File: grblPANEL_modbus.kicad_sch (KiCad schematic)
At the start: 16 parts, among them J401 Conn_01x02, U401 THVD1406

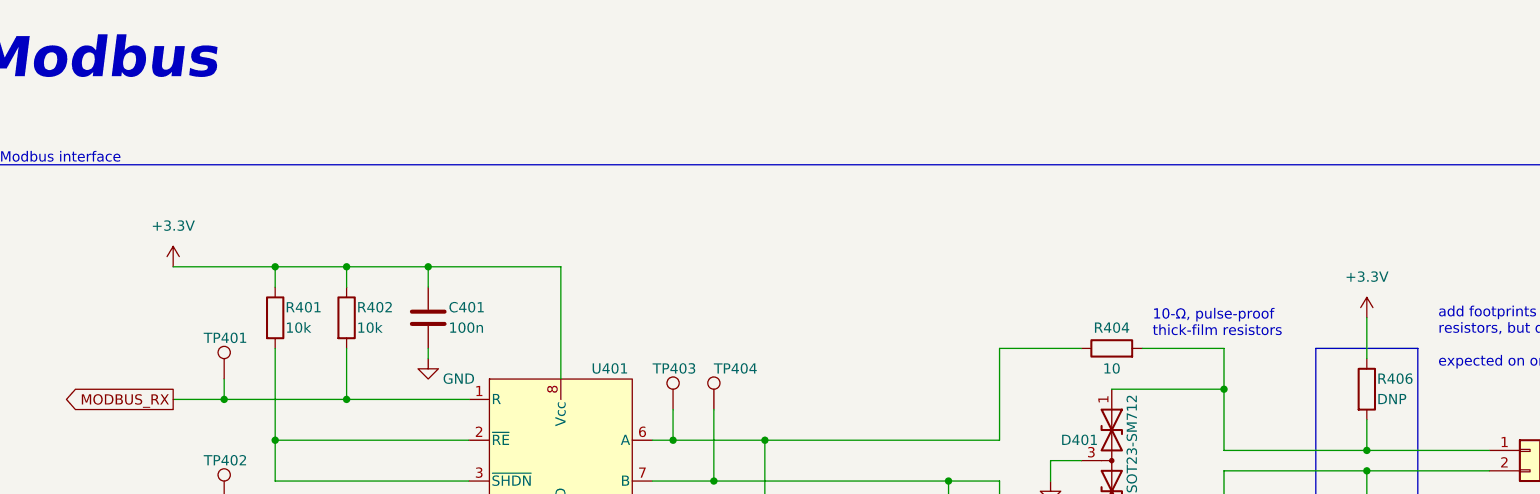
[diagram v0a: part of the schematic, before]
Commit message: ERC fixes
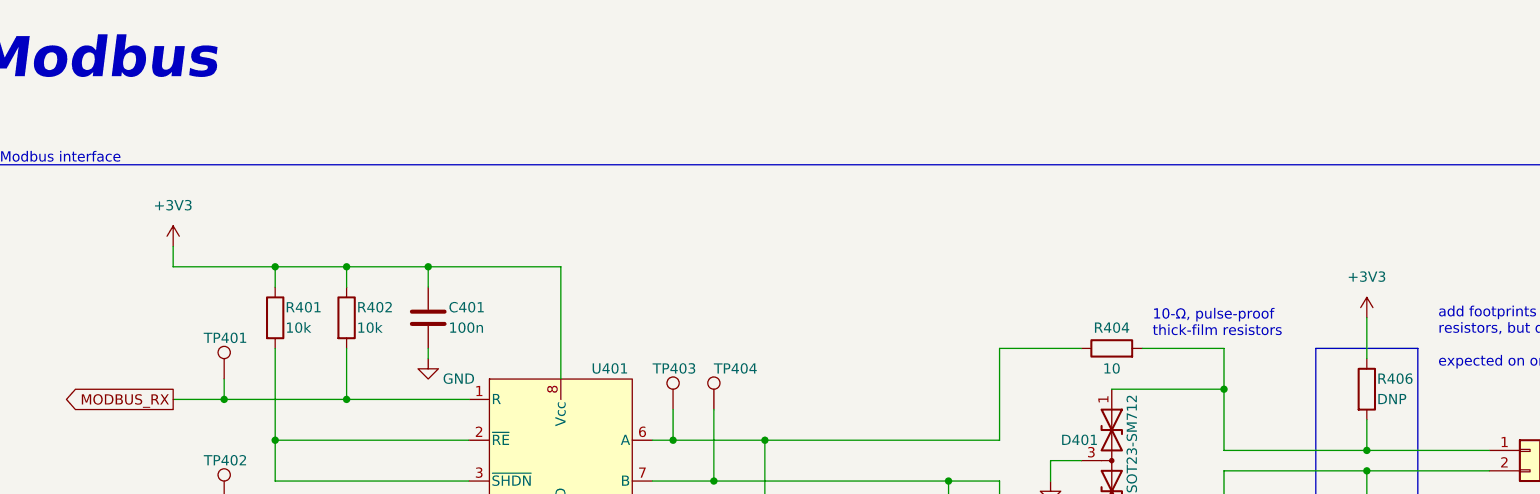
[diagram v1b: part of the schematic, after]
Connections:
- net +3.3V renamed +3V3
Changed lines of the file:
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@@
+    (stroke (width 0) (type default) (color 0 0 0 0))
+  )
+  (wire (pts (xy 62.23 49.53) (xy 62.23 52.07))
     (stroke (width 0) (type default) (color 0 0 0 0))
   )
@@
     (pin "1")
     (pin "2")
-  )
-  (symbol (lib_id "power:+3.3V") (at 210.82 58.42 0) (unit 1)
-    (in_bom yes) (on_board yes) (fields_autoplaced)
-    (property "Reference" "#PWR0405" (id 0) (at 210.82 62.23 0)
-      (effects (font (size 1.27 1.27)) hide)
-    )
-    (property "Value" "+3.3V" (id 1) (at 210.82 53.34 0))
-    (property "Footprint" "" (id 2) (at 210.82 58.42 0)
-      (effects (font (size 1.27 1.27)) hide)
-    )
-    (property "Datasheet" "" (id 3) (at 210.82 58.42 0)
-      (effects (font (size 1.27 1.27)) hide)
-    )
-    (pin "1")
   )
   (symbol (lib_id "Connector_Generic:Conn_01x02") (at 231.14 74.93 0) (unit 1)
@@
     (pin "1")
   )
+  (symbol (lib_id "power:+3V3") (at 62.23 49.53 0) (unit 1)
+    (in_bom yes) (on_board yes) (fields_autoplaced)
+    (property "Reference" "#PWR0108" (id 0) (at 62.23 53.34 0)
+      (effects (font (size 1.27 1.27)) hide)
+    )
+    (property "Value" "+3V3" (id 1) (at 62.23 44.45 0))
+    (property "Footprint" "" (id 2) (at 62.23 49.53 0)
+      (effects (font (size 1.27 1.27)) hide)
+    )
+    (property "Datasheet" "" (id 3) (at 62.23 49.53 0)
+      (effects (font (size 1.27 1.27)) hide)
+    )
+    (pin "1")
+  )
   (symbol (lib_id "Device:R") (at 179.07 62.23 90) (unit 1)
     (in_bom yes) (on_board yes)
@@
     (pin "3")
   )
-  (symbol (lib_id "power:+3.3V") (at 62.23 52.07 0) (unit 1)
-    (in_bom yes) (on_board yes) (fields_autoplaced)
-    (property "Reference" "#PWR0401" (id 0) (at 62.23 55.88 0)
-      (effects (font (size 1.27 1.27)) hide)
-    )
-    (property "Value" "+3.3V" (id 1) (at 62.23 46.99 0))
-    (property "Footprint" "" (id 2) (at 62.23 52.07 0)
-      (effects (font (size 1.27 1.27)) hide)
-    )
-    (property "Datasheet" "" (id 3) (at 62.23 52.07 0)
-      (effects (font (size 1.27 1.27)) hide)
-    )
-    (pin "1")
-  )
   (symbol (lib_id "Connector:TestPoint") (at 124.46 69.85 0) (unit 1)
     (in_bom yes) (on_board yes)
@@
     (pin "2")
   )
+  (symbol (lib_id "power:+3V3") (at 210.82 58.42 0) (unit 1)
+    (in_bom yes) (on_board yes) (fields_autoplaced)
+    (property "Reference" "#PWR0109" (id 0) (at 210.82 62.23 0)
+      (effects (font (size 1.27 1.27)) hide)
+    )
+    (property "Value" "+3V3" (id 1) (at 210.82 53.34 0))
+    (property "Footprint" "" (id 2) (at 210.82 58.42 0)
+      (effects (font (size 1.27 1.27)) hide)
+    )
+    (property "Datasheet" "" (id 3) (at 210.82 58.42 0)
+      (effects (font (size 1.27 1.27)) hide)
+    )
+    (pin "1")
+  )
   (symbol (lib_id "power:GND") (at 171.45 78.74 0) (unit 1)

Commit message: Refresh
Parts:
- C401: footprint (none) -> Capacitor_SMD:C_0603_1608Metric
- D401: footprint (none) -> Package_TO_SOT_SMD:SOT-23
- J401: footprint (none) -> TerminalBlock_4Ucon:TerminalBlock_4Ucon_1x02_P3.50mm_Horizontal
- JP401, TP401, TP402, TP403, TP404: footprint (none) -> Connector_Pin:Pin_D1.0mm_L10.0mm
- R401, R402, R403, R406, R407: footprint (none) -> Resistor_SMD:R_0603_1608Metric
- R404, R405: footprint (none) -> Resistor_SMD:R_1206_3216Metric
- U401: footprint (none) -> Package_SO:SOIC-8_3.9x4.9mm_P1.27mm
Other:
- note added: "1/2 watt termination resistor"
- note added: "Add footprints for 570 ohm bias resistors, but do not populate. Should be present on only one modbus node (usually master)."
- note added: "SM712 TVS - Vrwm -7v, +12v - Vbr -7.5v, +13.3v - Vc -10v, +19v (@ 1A) THVD106 - Max bus voltage +/- 12v - Peak bus voltage +/- 16v - ESD rated +/- 16kv"
- note added: "THVD1406 - 3.3v, auto switching (and mostly out of stock..) Enable auto-direction mode by tying SHDN and RE pins together to logic high"
- note added: "THVD1406 - 3.3v, auto switching, mostly out of stock.."
- note removed: "Enable auto-direction mode by tying SHDN and RE pins together to logic high"
- note removed: "THVD1406 - 3.3v, auto switching, mostly out of stock.. todo: take a closer look at the circuitry of existing AliExpress adapter"
- note removed: "add footprints for 570 ohm bias resistors, but do not populate. expected on only single (master) node"
- moved on the sheet: D401, J401, R404, R405, R406, R407

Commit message: PCB layout - WIP
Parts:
- J401: footprint TerminalBlock_4Ucon:TerminalBlock_4Ucon_1x02_P3.50mm_Horizontal -> TerminalBlock_Phoenix:TerminalBlock_Phoenix_PT-1,5-2-3.5-H_1x02_P3.50mm_Horizontal
- JP401: footprint Connector_Pin:Pin_D1.0mm_L10.0mm -> Connector_PinHeader_2.54mm:PinHeader_1x02_P2.54mm_Vertical
- TP401, TP402, TP403, TP404: footprint Connector_Pin:Pin_D1.0mm_L10.0mm -> TestPoint:TestPoint_THTPad_D2.0mm_Drill1.0mm
- renumbered R406 to R404, R407 to R405, R404 to R406, R405 to R407
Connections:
- net CONN_RS485_A: now reaches D401.1 (A1), J401.1 (Pin_1), R406.2
- net CONN_RS485_A: no longer R404.2
- net CONN_RS485_B: now reaches D401.2 (A2), J401.2 (Pin_2), R407.2
- net CONN_RS485_B: no longer R405.1
- net RS485_B: now reaches JP401.2 (B), R407.1, TP404.1, U401.7 (B)
- net RS485_B: now also R405.1
- net RS485_MODE_SELECT: now reaches R401.2, U401.2 (~{RE}), U401.3 (~{SHDN})
- net RS485_A: now reaches R403.1, R406.1, TP403.1, U401.6 (A)
- net RS485_A: now also R404.2
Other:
- moved on the sheet: D401, J401, R404, R405, R406, R407

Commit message: modbus cleanup
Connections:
- net CONN_RS485_A: now also D401.2 (A2); no longer D401.1 (A1)
- net CONN_RS485_B: now also D401.1 (A1); no longer D401.2 (A2)
- net RS485_A: now also JP401.1 (A); no longer R403.1
- net RS485_B: now also R403.2; no longer JP401.2 (B)
- new net: JP401.2 (B), R403.1
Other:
- moved on the sheet: JP401, R403
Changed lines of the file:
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@@
     (stroke (width 0) (type default) (color 0 0 0 0))
   )
-  (wire (pts (xy 144.78 85.09) (xy 147.32 85.09))
+  (wire (pts (xy 147.32 85.09) (xy 149.86 85.09))
     (stroke (width 0) (type default) (color 0 0 0 0))
   )
@@
     (pin "8")
   )
-  (symbol (lib_id "Device:R") (at 140.97 85.09 90) (unit 1)
-    (in_bom yes) (on_board yes)
-    (property "Reference" "R403" (id 0) (at 140.97 82.55 90))
-    (property "Value" "120" (id 1) (at 140.97 87.63 90))
-    (property "Footprint" "Resistor_SMD:R_0603_1608Metric" (id 2) (at 140.97 86.868 90)
-      (effects (font (size 1.27 1.27)) hide)
-    )
-    (property "Datasheet" "~" (id 3) (at 140.97 85.09 0)
+  (symbol (lib_id "Device:R") (at 153.67 85.09 90) (unit 1)
+    (in_bom yes) (on_board yes)
+    (property "Reference" "R403" (id 0) (at 153.67 82.55 90))
+    (property "Value" "120" (id 1) (at 153.67 87.63 90))
+    (property "Footprint" "Resistor_SMD:R_0603_1608Metric" (id 2) (at 153.67 86.868 90)
+      (effects (font (size 1.27 1.27)) hide)
+    )
+    (property "Datasheet" "~" (id 3) (at 153.67 85.09 0)
       (effects (font (size 1.27 1.27)) hide)
     )
@@
     (pin "1")
   )
-  (symbol (lib_id "Device:D_TVS_Dual_AAC") (at 208.28 76.2 270) (unit 1)
-    (in_bom yes) (on_board yes)
-    (property "Reference" "D401" (id 0) (at 201.93 73.66 90)
-      (effects (font (size 1.27 1.27)) (justify left))
-    )
-    (property "Value" "CDSOT23-SM712" (id 1) (at 210.82 67.945 0)
-      (effects (font (size 1.27 1.27)) (justify left))
-    )
-    (property "Footprint" "Package_TO_SOT_SMD:SOT-23" (id 2) (at 208.28 72.39 0)
-      (effects (font (size 1.27 1.27)) hide)
-    )
-    (property "Datasheet" "~" (id 3) (at 208.28 72.39 0)
+  (symbol (lib_id "Device:D_TVS_Dual_AAC") (at 208.28 76.2 270) (mirror x) (unit 1)
+    (in_bom yes) (on_board yes)
+    (property "Reference" "D401" (id 0) (at 201.93 78.74 90)
+      (effects (font (size 1.27 1.27)) (justify left))
+    )
+    (property "Value" "CDSOT23-SM712" (id 1) (at 210.82 84.455 0)
+      (effects (font (size 1.27 1.27)) (justify left))
+    )
+    (property "Footprint" "Package_TO_SOT_SMD:SOT-23" (id 2) (at 208.28 80.01 0)
+      (effects (font (size 1.27 1.27)) hide)
+    )
+    (property "Datasheet" "~" (id 3) (at 208.28 80.01 0)
       (effects (font (size 1.27 1.27)) hide)
     )
@@
     (pin "2")
   )
-  (symbol (lib_id "Jumper:Jumper_2_Bridged") (at 152.4 85.09 0) (unit 1)
-    (in_bom yes) (on_board yes)
-    (property "Reference" "JP401" (id 0) (at 152.4 82.55 0))
-    (property "Value" "Jumper_2_Bridged" (id 1) (at 156.21 87.63 0)
-      (effects (font (size 1.27 1.27)) hide)
-    )
-    (property "Footprint" "Connector_PinHeader_2.54mm:PinHeader_1x02_P2.54mm_Vertical" (id 2) (at 152.4 85.09 0)
-      (effects (font (size 1.27 1.27)) hide)
-    )
-    (property "Datasheet" "~" (id 3) (at 152.4 85.09 0)
-      (effects (font (size 1.27 1.27)) hide)
-    )
+  (symbol (lib_id "Jumper:Jumper_2_Bridged") (at 142.24 85.09 0) (unit 1)
+    (in_bom yes) (on_board yes)
+    (property "Reference" "JP401" (id 0) (at 142.24 82.55 0))
+    (property "Value" "Jumper_2_Bridged" (id 1) (at 146.05 87.63 0)
+      (effects (font (size 1.27 1.27)) hide)
+    )
+    (property "Footprint" "Connector_PinHeader_2.54mm:PinHeader_1x02_P2.54mm_Vertical" (id 2) (at 142.24 85.09 0)
+      (effects (font (size 1.27 1.27)) hide)
+    )
+    (property "Datasheet" "~" (id 3) (at 142.24 85.09 0)
+      (effects (font (size 1.27 1.27)) hide)
+    )

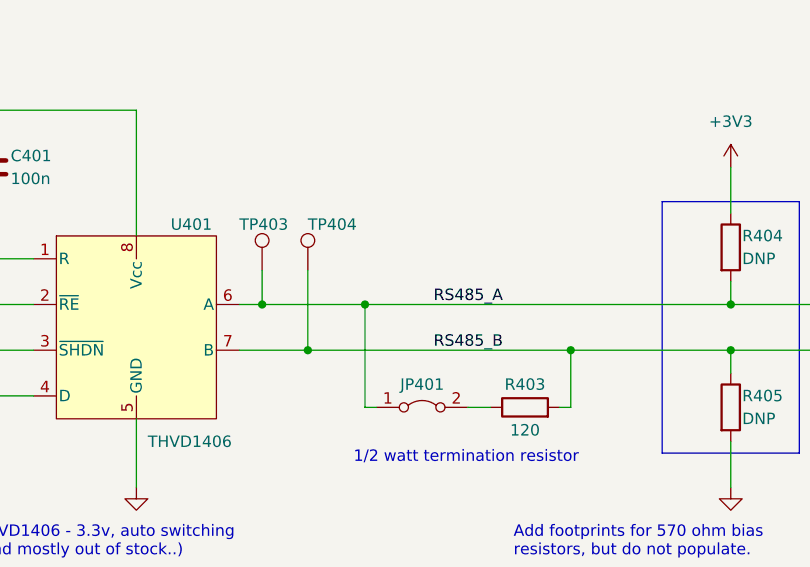
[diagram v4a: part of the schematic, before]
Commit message: canbus & modbus test points
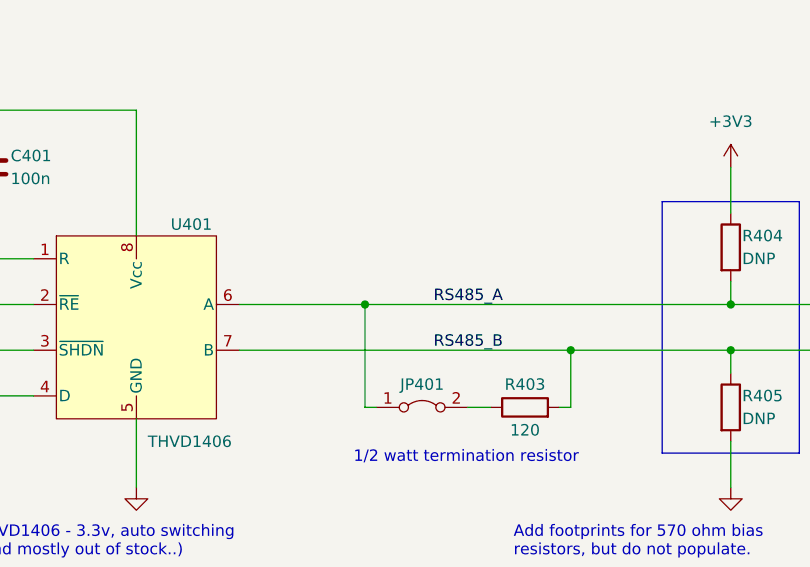
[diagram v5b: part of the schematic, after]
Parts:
- removed TP403, TP404: TestPoint, TestPoint:TestPoint_THTPad_D2.0mm_Drill1.0mm, symbol Connector:TestPoint
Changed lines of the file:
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@@
   (junction (at 74.93 73.66) (diameter 0) (color 0 0 0 0)
   )
-  (junction (at 129.54 78.74) (diameter 0) (color 0 0 0 0)
-  )
   (junction (at 68.58 83.82) (diameter 0) (color 0 0 0 0)
   )
@@
   (junction (at 222.25 67.31) (diameter 0) (color 0 0 0 0)
   )
-  (junction (at 124.46 73.66) (diameter 0) (color 0 0 0 0)
-  )
   (junction (at 83.82 68.58) (diameter 0) (color 0 0 0 0)
   )
@@
     (stroke (width 0) (type default) (color 0 0 0 0))
   )
-  (wire (pts (xy 129.54 69.85) (xy 129.54 78.74))
-    (stroke (width 0) (type default) (color 0 0 0 0))
-  )
   (wire (pts (xy 74.93 62.23) (xy 74.93 73.66))
     (stroke (width 0) (type default) (color 0 0 0 0))
@@
     (stroke (width 0) (type default) (color 0 0 0 0))
   )
-  (wire (pts (xy 121.92 73.66) (xy 124.46 73.66))
-    (stroke (width 0) (type default) (color 0 0 0 0))
-  )
   (wire (pts (xy 135.89 85.09) (xy 137.16 85.09))
     (stroke (width 0) (type default) (color 0 0 0 0))
@@
     (stroke (width 0) (type default) (color 0 0 0 0))
   )
-  (wire (pts (xy 121.92 78.74) (xy 129.54 78.74))
+  (wire (pts (xy 121.92 78.74) (xy 158.75 78.74))
     (stroke (width 0) (type default) (color 0 0 0 0))
   )
@@
     (stroke (width 0) (type default) (color 0 0 0 0))
   )
-  (wire (pts (xy 124.46 73.66) (xy 135.89 73.66))
-    (stroke (width 0) (type default) (color 0 0 0 0))
-  )
-  (wire (pts (xy 129.54 78.74) (xy 158.75 78.74))
+  (wire (pts (xy 121.92 73.66) (xy 135.89 73.66))
     (stroke (width 0) (type default) (color 0 0 0 0))
   )
@@
   )
   (wire (pts (xy 176.53 58.42) (xy 176.53 63.5))
-    (stroke (width 0) (type default) (color 0 0 0 0))
-  )
-  (wire (pts (xy 124.46 69.85) (xy 124.46 73.66))
     (stroke (width 0) (type default) (color 0 0 0 0))
   )
@@
     (pin "1")
   )
-  (symbol (lib_id "Connector:TestPoint") (at 129.54 69.85 0) (unit 1)
-    (in_bom yes) (on_board yes)
-    (property "Reference" "TP404" (id 0) (at 129.54 64.77 0)
-      (effects (font (size 1.27 1.27)) (justify left))
-    )
-    (property "Value" "TestPoint" (id 1) (at 132.08 67.8179 0)
-      (effects (font (size 1.27 1.27)) (justify left) hide)
-    )
-    (property "Footprint" "TestPoint:TestPoint_THTPad_D2.0mm_Drill1.0mm" (id 2) (at 134.62 69.85 0)
-      (effects (font (size 1.27 1.27)) hide)
-    )
-    (property "Datasheet" "~" (id 3) (at 134.62 69.85 0)
-      (effects (font (size 1.27 1.27)) hide)
-    )
-    (pin "1")
-  )
   (symbol (lib_id "Device:D_TVS_Dual_AAC") (at 208.28 76.2 270) (mirror x) (unit 1)
     (in_bom yes) (on_board yes)
@@
     (pin "3")
   )
-  (symbol (lib_id "Connector:TestPoint") (at 124.46 69.85 0) (unit 1)
-    (in_bom yes) (on_board yes)
-    (property "Reference" "TP403" (id 0) (at 121.92 64.77 0)
-      (effects (font (size 1.27 1.27)) (justify left))
-    )
-    (property "Value" "TestPoint" (id 1) (at 127 67.8179 0)
-      (effects (font (size 1.27 1.27)) (justify left) hide)
-    )
-    (property "Footprint" "TestPoint:TestPoint_THTPad_D2.0mm_Drill1.0mm" (id 2) (at 129.54 69.85 0)
-      (effects (font (size 1.27 1.27)) hide)
-    )
-    (property "Datasheet" "~" (id 3) (at 129.54 69.85 0)
-      (effects (font (size 1.27 1.27)) hide)
-    )
-    (pin "1")
-  )
   (symbol (lib_id "Device:R") (at 83.82 58.42 0) (unit 1)

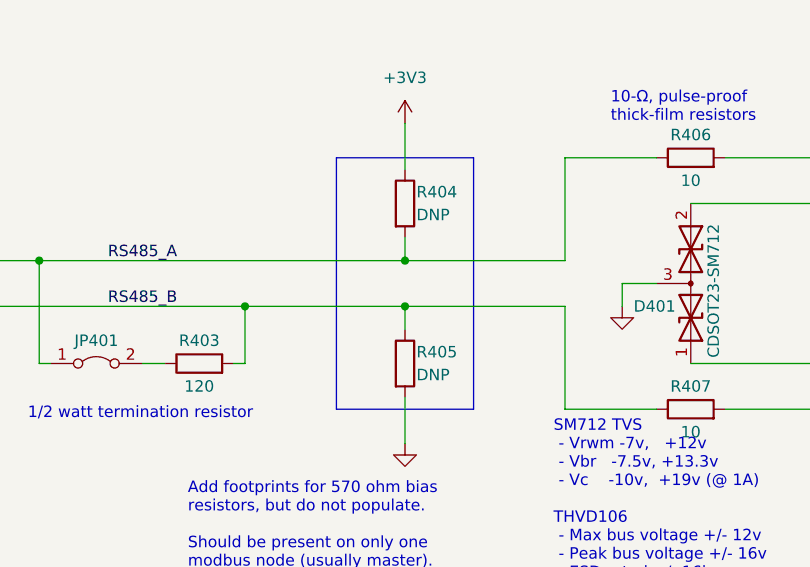
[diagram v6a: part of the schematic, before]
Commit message: Board changes for Rev B
Import changes from schematic.

Place and route changes from schematic:
Headers for serial console.
DNP components to v7 format.
Power status components.
LEDs to bottom side, plus silkscreen.

Update schematic page settings (RevB).

Update PCB page settings (RevB).

Silkscreen & test point tweaks.
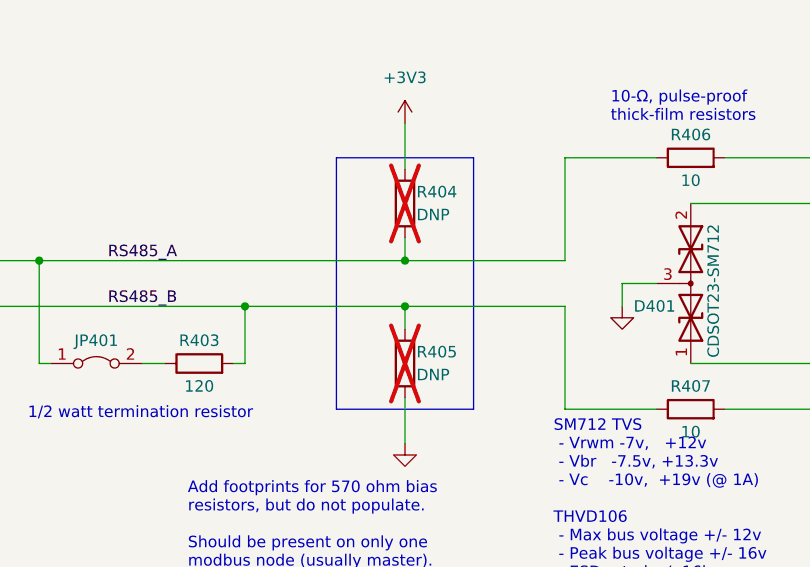
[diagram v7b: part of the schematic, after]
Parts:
- R404, R405: now not fitted
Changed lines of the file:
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@@
     (title "grblPANEL")
     (date "2022-12-12")
-    (rev "0.1")
+    (rev "B")
     (company "dresco")
   )
@@
   )
   (symbol (lib_id "Device:R") (at 176.53 67.31 0) (unit 1)
-    (in_bom yes) (on_board yes) (dnp no)
+    (in_bom yes) (on_board yes) (dnp yes)
     (property "Reference" "R404" (at 177.8 66.04 0)
       (effects (font (size 1.27 1.27)) (justify left))
@@
   )
   (symbol (lib_id "Device:R") (at 176.53 85.09 0) (unit 1)
-    (in_bom yes) (on_board yes) (dnp no)
+    (in_bom yes) (on_board yes) (dnp yes)
     (property "Reference" "R405" (at 177.8 83.82 0)
       (effects (font (size 1.27 1.27)) (justify left))
